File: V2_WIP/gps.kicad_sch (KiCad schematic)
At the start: 36 parts, among them U10 24C32, U101 DFR0654, U102 W25Q128JFV, U2 TPS613222ADBVR

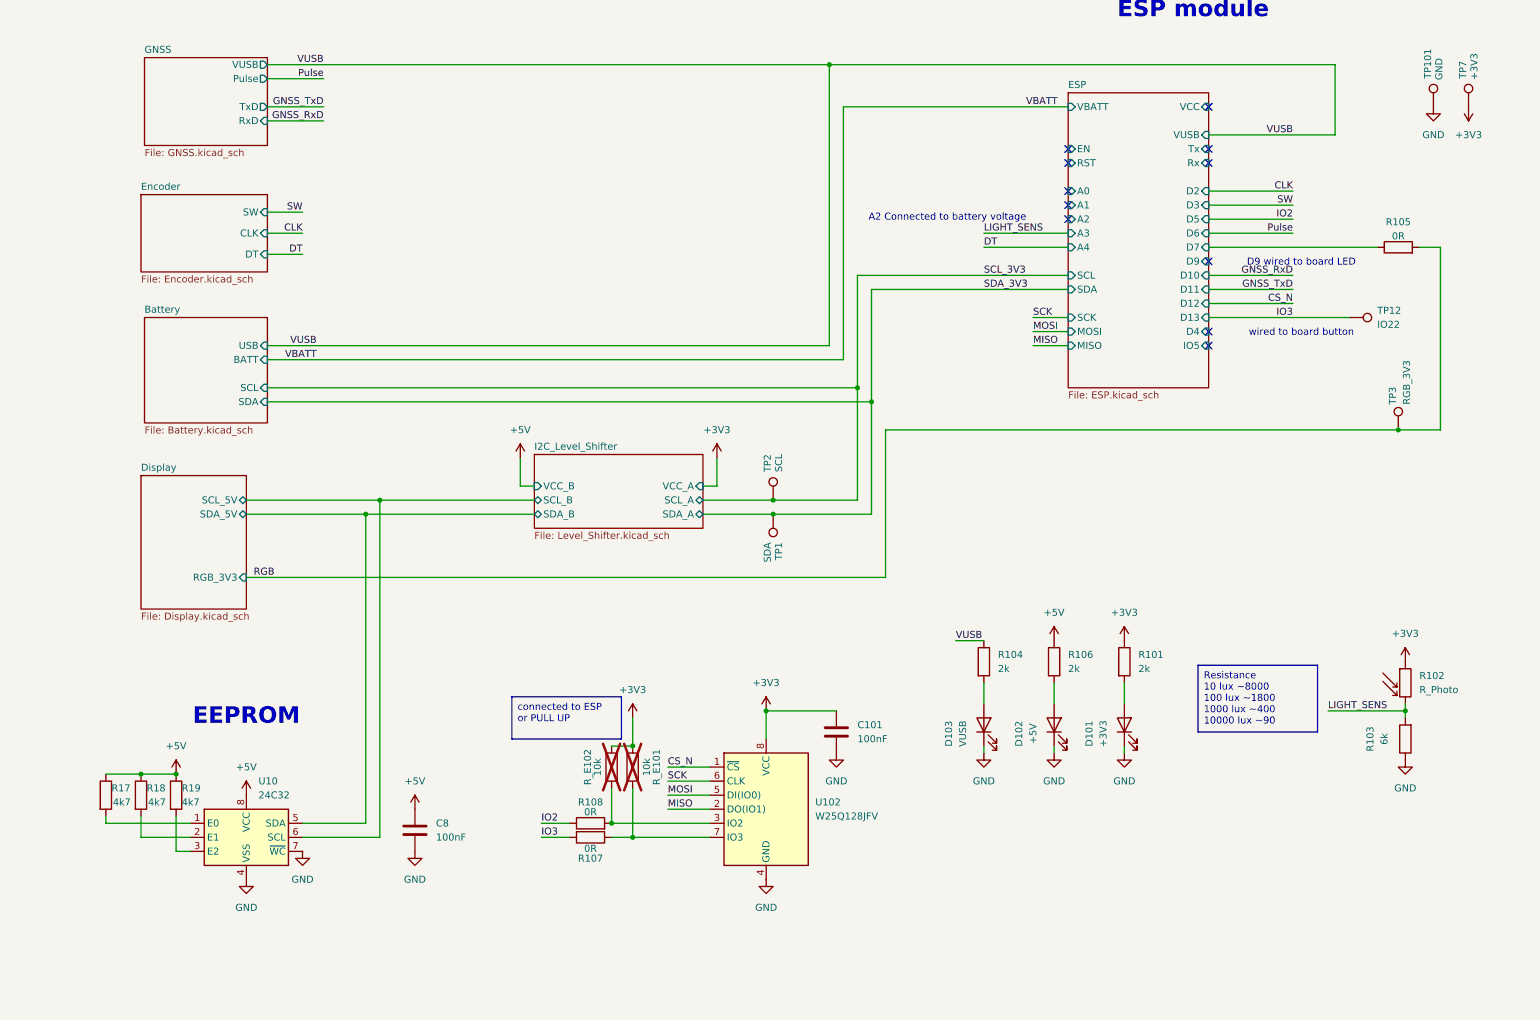
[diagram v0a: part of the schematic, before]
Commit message: Removed EEPROM, Adjusted Flash connection, renamed ESP pins and several other signals
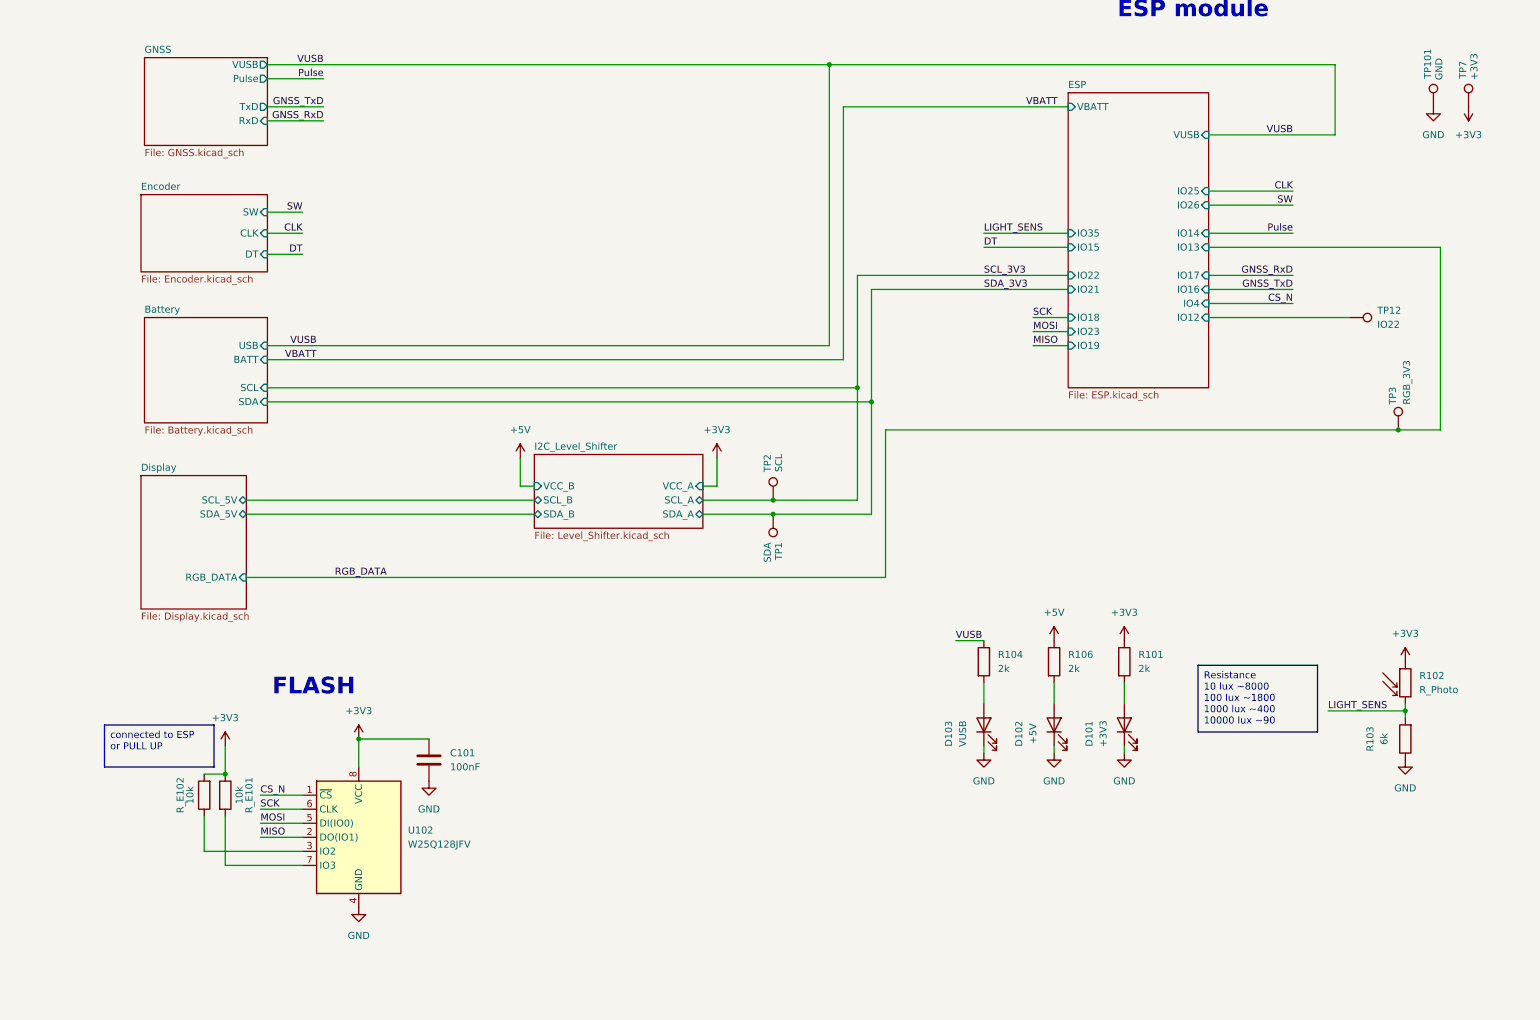
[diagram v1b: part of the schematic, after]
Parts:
- removed C8: 100nF, Capacitor_SMD:C_0805_2012Metric_Pad1.18x1.45mm_HandSolder, symbol Device:C
- removed R105, R107, R108: 0R, Resistor_SMD:R_0603_1608Metric_Pad0.98x0.95mm_HandSolder, symbol Device:R
- removed R17, R18, R19: 4k7, Resistor_SMD:R_0603_1608Metric_Pad0.98x0.95mm_HandSolder, symbol Device:R
- removed U10: 24C32, Package_SO:SOIC-8_3.9x4.9mm_P1.27mm, symbol Memory_EEPROM:M24C01-FMN
- R_E101, R_E102: now fitted
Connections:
- net IO3 renamed ESP/IO12
- net RGB renamed RGB_DATA
- no-connect marks 39 -> 28
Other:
- sheet Display ports: added RGB_DATA; removed RGB_3V3
- sheet ESP ports: added IO12, IO13, IO14, IO15, IO16, IO17, IO18, IO19, IO21, IO22, IO23, IO25, IO26, IO35, IO4; removed A0, A1, A2, A3, A4, D10, D11, D12, D13, D2, D3, D4, D5, D6, D7, D9, EN, IO5, MISO, MOSI, RST, Rx, SCK, SCL, SDA, Tx, VCC
- note added: "FLASH"
- note removed: "A2 Connected to battery voltage"
- note removed: "D9 wired to board LED"
- note removed: "EEPROM"
- note removed: "wired to board button"
- moved on the sheet: C101, U102

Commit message: minor changes
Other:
- moved on the sheet: TP12, TP3

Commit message: finallizes schematic; pcb progress
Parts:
- removed C102: 470u, Capacitor_SMD:C_0603_1608Metric_Pad1.08x0.95mm_HandSolder, symbol Device:C
- removed C4, C5, C6: 10uF, Capacitor_SMD:C_0603_1608Metric_Pad1.08x0.95mm_HandSolder, symbol Device:C
- removed D2: B120-E3, Diode_SMD:D_SMA, symbol Diode:B120-E3
- removed L1: 2.2 uH, Inductor_SMD:L_1008_2520Metric_Pad1.43x2.20mm_HandSolder, symbol Device:L
- removed R1: 0R, Resistor_SMD:R_0805_2012Metric_Pad1.20x1.40mm_HandSolder, symbol Device:R
- removed TP5: +5V, TestPoint:TestPoint_Pad_D1.5mm, symbol Connector:TestPoint
- removed U2: TPS613222ADBVR, Package_TO_SOT_SMD:SOT-23-5, symbol Regulator_Switching:TPS613226ADBV
- added C103, C104: 100nF, Capacitor_SMD:C_0805_2012Metric_Pad1.18x1.45mm_HandSolder, symbol Device:C
- added TP102: IMU_INT, TestPoint:TestPoint_Pad_D1.5mm, symbol Connector:TestPoint
- added TP103: +5V, TestPoint:TestPoint_Pad_D1.5mm, symbol Connector:TestPoint
- added U103: ICM-45686, Package_LGA:LGA-14_3x2.5mm_P0.5mm_LayoutBorder3x4y, symbol icm-45686:ICM-45686
- R102: value R_Photo -> NSL-A95011
- R103: value 6k -> 56k
- TP12: value IO22 -> IO12
- TP3: value RGB_3V3 -> RGB_DATA
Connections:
- net +3V3: now also R103.2, C103.2, C104.2, U103.5 (VDDIO), U103.8 (VDD); no longer R102.1
- net +5V: now also TP103.1
- net GND: now also R102.2, C103.1, C104.1, U103.6 (GND); no longer R103.1
- net LIGHT_SENS: now also R102.1, R103.1; no longer R102.2, R103.2
- net MISO: now also U103.1 (SDO/AD0)
- net MOSI: now also U103.14 (SDI/SDA)
- net SCK: now also U103.13 (CLK/SCL)
- net CS_N renamed SEL_FL
- new net: TP102.1, U103.4 (INT)
- new net SEL_IMU: U103.12 (CS)
- no-connect marks 28 -> 34
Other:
- sheet ESP ports: added IO27, IO32; removed IO15
- note added: "IMU"
- note removed: "DC/DC"
- moved on the sheet: C101, D101, D102, D103, R101, R104, R106

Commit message: updated most datashets
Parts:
- removed U101: DFR0654, DFR0654:DFR0654_2, symbol DFR0654:DFR0654
- C101, C103, C104: footprint Capacitor_SMD:C_0805_2012Metric_Pad1.18x1.45mm_HandSolder -> Capacitor_SMD:C_0603_1608Metric_Pad1.08x0.95mm_HandSolder
- U102: value W25Q128JFV -> *W25Q128JFV
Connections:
- no-connect marks 34 -> 6

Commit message: up to date i dont remember what changed
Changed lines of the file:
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@@
 (kicad_sch
-	(version 20231120)
+	(version 20250114)
 	(generator "eeschema")
-	(generator_version "8.0")
+	(generator_version "9.0")
 	(paper "A4")
 	(title_block
@@
 		(rev "1")
 	)
+	(text "ESP module"
+		(exclude_from_sim no)
+		(at 208.28 17.78 0)
+		(effects
+			(font
+				(size 3 3)
+				(bold yes)
+			)
+		)
+	)
+	(text "FLASH"
+		(exclude_from_sim no)
+		(at 60.452 140.462 0)
+		(effects
+			(font
+				(size 3 3)
+				(bold yes)
+			)
+		)
+	)
+	(text "IMU"
+		(exclude_from_sim no)
+		(at 132.334 138.938 0)
+		(effects
+			(font
+				(size 3 3)
+				(bold yes)
+			)
+		)
+	)
+	(text_box "connected to ESP or PULL UP"
+		(exclude_from_sim no)
+		(at 20.574 147.32 0)
+		(size 19.812 7.62)
+		(margins 0.9525 0.9525 0.9525 0.9525)
+		(stroke
+			(width 0)
+			(type default)
+		)
+		(fill
+			(type none)
+		)
+		(effects
+			(font
+				(size 1.27 1.27)
+			)
+			(justify left top)
+		)
+	)
 	(junction
 		(at 158.75 86.36)
@@
 		)
 	)
-	(text_box "connected to ESP or PULL UP"
-		(exclude_from_sim no)
-		(at 20.574 147.32 0)
-		(size 19.812 7.62)
-		(stroke
-			(width 0)
-			(type default)
-		)
-		(fill
-			(type none)
-		)
-		(effects
-			(font
-				(size 1.27 1.27)
-			)
-			(justify left top)
-		)
-	)
-	(text "ESP module"
-		(exclude_from_sim no)
-		(at 208.28 17.78 0)
-		(effects
-			(font
-				(size 3 3)
-				(bold yes)
-			)
-		)
-	)
-	(text "FLASH"
-		(exclude_from_sim no)
-		(at 60.452 140.462 0)
-		(effects
-			(font
-				(size 3 3)
-				(bold yes)
-			)
-		)
-	)
-	(text "IMU"
-		(exclude_from_sim no)
-		(at 132.334 138.938 0)
-		(effects
-			(font
-				(size 3 3)
-				(bold yes)
-			)
-		)
-	)
 	(label "SW"
 		(at 181.61 54.61 0)
-		(fields_autoplaced yes)
 		(effects
 			(font
@@
 	(label "DT"
 		(at 181.61 62.23 0)
-		(fields_autoplaced yes)
 		(effects
 			(font
@@
 	(label "MISO"
 		(at 181.61 93.98 0)
-		(fields_autoplaced yes)
 		(effects
 			(font
@@
 	(label "MISO"
 		(at 111.76 160.02 0)
-		(fields_autoplaced yes)
 		(effects
 			(font
@@
 	(label "VBATT"
 		(at 181.61 67.31 0)
-		(fields_autoplaced yes)
 		(effects
 			(font
@@
 	(label "SCL_3V3"
 		(at 181.61 74.93 0)
-		(fields_autoplaced yes)
 		(effects
 			(font
@@
 	(label "MOSI"
 		(at 124.46 148.59 0)
-		(fields_autoplaced yes)
 		(effects
 			(font
@@
 	(label "SCK"
 		(at 50.8 162.56 0)
-		(fields_autoplaced yes)
 		(effects
 			(font
@@
 	(label "MOSI"
 		(at 50.8 165.1 0)
-		(fields_autoplaced yes)
 		(effects
 			(font
@@
 	(label "MISO"
 		(at 50.8 167.64 0)
-		(fields_autoplaced yes)
 		(effects
 			(font
@@
 	(label "CLK"
 		(at 181.61 58.42 0)
-		(fields_autoplaced yes)
 		(effects
 			(font
@@
 	(label "SEL_IMU"
 		(at 181.61 83.82 0)
-		(fields_autoplaced yes)
 		(effects
 			(font
@@
 	(label "SDA_3V3"
 		(at 181.61 77.47 0)
-		(fields_autoplaced yes)
 		(effects
 			(font
@@
 	(label "SEL_FL"
 		(at 50.8 160.02 0)
-		(fields_autoplaced yes)
 		(effects
 			(font
@@
 	(label "LIGHT_SENS"
 		(at 236.22 53.34 180)
-		(fields_autoplaced yes)
 		(effects
 			(font
@@
 	(label "SEL_IMU"
 		(at 124.46 143.51 0)
-		(fields_autoplaced yes)
 		(effects
 			(font
@@
 	(label "GNSS_TxD"
 		(at 181.61 35.56 0)
-		(fields_autoplaced yes)
 		(effects
 			(font
@@
 	(label "SCK"
 		(at 181.61 88.9 0)
-		(fields_autoplaced yes)
 		(effects
 			(font
@@
 	(label "SCK"
 		(at 124.46 146.05 0)
-		(fields_autoplaced yes)
 		(effects
 			(font
@@
 	(label "MOSI"
 		(at 181.61 91.44 0)
-		(fields_autoplaced yes)
 		(effects
 			(font
@@
 	(label "Pulse"
 		(at 181.61 30.48 0)
-		(fields_autoplaced yes)
 		(effects
 			(font
@@
 	(label "VUSB"
 		(at 181.61 27.94 0)
-		(fields_autoplaced yes)
 		(effects
 			(font
@@
 	(label "VUSB"
 		(at 185.42 132.08 0)
-		(fields_autoplaced yes)
 		(effects
 			(font
@@
 	(label "GNSS_RxD"
 		(at 181.61 38.1 0)
-		(fields_autoplaced yes)
 		(effects
 			(font
@@
 	(label "RGB_DATA"
 		(at 73.66 120.65 180)
-		(fields_autoplaced yes)
 		(effects
 			(font
@@
 	(label "LIGHT_SENS"
 		(at 243.84 144.78 0)
-		(fields_autoplaced yes)
 		(effects
 			(font
@@
 	(label "SEL_FL"
 		(at 181.61 86.36 0)
-		(fields_autoplaced yes)
 		(effects
 			(font
@@
 		(at 29.845 73.66)
 		(size 22.225 19.05)
+		(exclude_from_sim no)
+		(in_bom yes)
+		(on_board yes)
+		(dnp no)
 		(fields_autoplaced yes)
 		(stroke
@@
 		(at 29.845 26.67)
 		(size 22.225 15.875)
+		(exclude_from_sim no)
+		(in_bom yes)
+		(on_board yes)
+		(dnp no)
 		(fields_autoplaced yes)
 		(stroke
@@
 		(at 29.21 51.435)
 		(size 22.86 13.97)
+		(exclude_from_sim no)
+		(in_bom yes)
+		(on_board yes)
+		(dnp no)
 		(fields_autoplaced yes)
 		(stroke
@@
 		(at 29.21 102.235)
 		(size 19.05 24.13)
+		(exclude_from_sim no)
+		(in_bom yes)
+		(on_board yes)
+		(dnp no)
 		(fields_autoplaced yes)
 		(stroke
@@
 		(at 196.85 24.892)
 		(size 25.4 72.898)
+		(exclude_from_sim no)
+		(in_bom yes)
+		(on_board yes)
+		(dnp no)
 		(fields_autoplaced yes)
 		(stroke
@@
 		(at 100.33 98.425)
 		(size 30.48 13.335)
+		(exclude_from_sim no)
+		(in_bom yes)
+		(on_board yes)
+		(dnp no)
 		(fields_autoplaced yes)
 		(stroke
@@
 		)
 	)
+	(embedded_fonts no)
 )
